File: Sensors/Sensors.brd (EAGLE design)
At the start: 101.6 x 53.3 mm, 28 parts, among them J10 JST_CONNECTOR, J11 JST_CONNECTOR, J2 JST_CONNECTOR, J5 JST_CONNECTOR, J6 JST_CONNECTOR, J7 JST_CONNECTOR, J8 JST_CONNECTOR, J9 JST_CONNECTOR

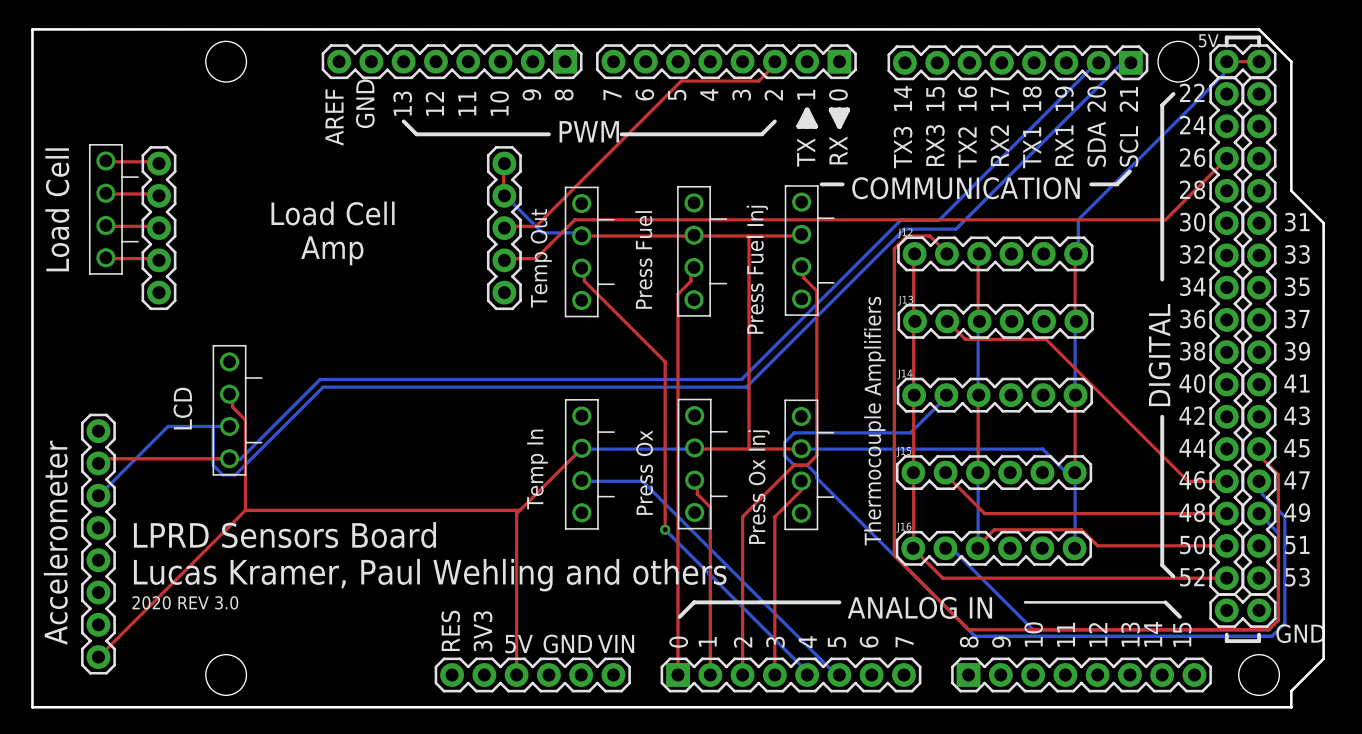
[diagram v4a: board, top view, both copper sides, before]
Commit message: Some minor tweaks to the layout
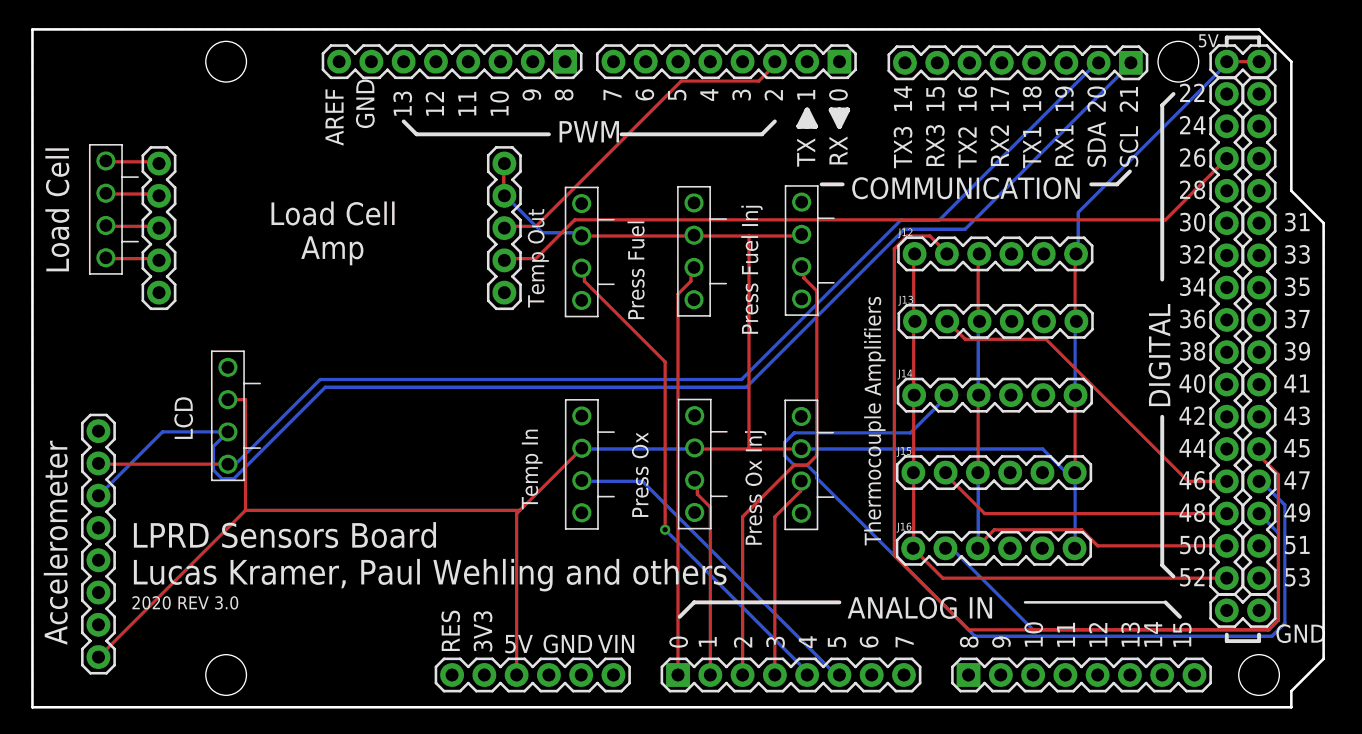
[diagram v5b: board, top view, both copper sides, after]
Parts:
- moved J11 0.45 mm to (15.4, 24.2)
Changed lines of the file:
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@@
 Lucas Kramer, Paul Wehling and others</text>
 <text x="7.7724" y="7.7089" size="1.016" layer="21" font="vector" ratio="15">2020 REV 3.0</text>
-<text x="48.7553" y="31.2039" size="1.27" layer="21" font="vector" ratio="15" rot="R90">Press Fuel</text>
-<text x="48.8061" y="14.986" size="1.27" layer="21" font="vector" ratio="15" rot="R90">Press Ox</text>
-<text x="40.5003" y="31.4579" size="1.27" layer="21" font="vector" ratio="15" rot="R90">Temp Out</text>
-<text x="40.1955" y="15.5829" size="1.27" layer="21" font="vector" ratio="15" rot="R90">Temp In</text>
+<text x="48.1457" y="30.3911" size="1.27" layer="21" font="vector" ratio="15" rot="R90">Press Fuel</text>
+<text x="48.4632" y="14.8209" size="1.27" layer="21" font="vector" ratio="15" rot="R90">Press Ox</text>
+<text x="40.2717" y="31.4579" size="1.27" layer="21" font="vector" ratio="15" rot="R90">Temp Out</text>
+<text x="39.7764" y="15.5829" size="1.27" layer="21" font="vector" ratio="15" rot="R90">Temp In</text>
 <text x="23.6474" y="35.2806" size="1.778" layer="21" font="vector" ratio="15" align="bottom-center">Load Cell
 Amp</text>
 <text x="2.8702" y="34.0868" size="1.778" layer="21" font="vector" ratio="15" rot="R90">Load Cell</text>
 <text x="2.7432" y="4.9022" size="1.778" layer="21" font="vector" ratio="15" rot="R90">Accelerometer</text>
-<text x="57.5183" y="29.2354" size="1.27" layer="21" font="vector" ratio="15" rot="R90">Press Fuel Inj</text>
-<text x="57.658" y="12.7" size="1.27" layer="21" font="vector" ratio="15" rot="R90">Press Ox Inj</text>
-<text x="12.5476" y="21.6916" size="1.4224" layer="21" font="vector" ratio="15" rot="R90">LCD</text>
+<text x="57.0992" y="29.2354" size="1.27" layer="21" font="vector" ratio="15" rot="R90">Press Fuel Inj</text>
+<text x="57.3913" y="12.6365" size="1.27" layer="21" font="vector" ratio="15" rot="R90">Press Ox Inj</text>
+<text x="12.6111" y="20.9423" size="1.4224" layer="21" font="vector" ratio="15" rot="R90">LCD</text>
 <text x="66.7639" y="12.7381" size="1.27" layer="21" font="vector" ratio="15" rot="R90">Thermocouple Amplifiers</text>
 </plain>
@@
 <element name="J5" library="LPRD_RELAY" package="B4B-XH-A(LF)(SN)" value="JST_CONNECTOR" x="60.5282" y="37.211" smashed="yes" rot="R90"/>
 <element name="J10" library="LPRD_RELAY" package="B4B-XH-A(LF)(SN)" value="JST_CONNECTOR" x="60.5028" y="20.3454" smashed="yes" rot="R90"/>
-<element name="J11" library="LPRD_RELAY" package="B4B-XH-A(LF)(SN)" value="JST_CONNECTOR" x="15.5067" y="24.638" smashed="yes" rot="R90"/>
+<element name="J11" library="LPRD_RELAY" package="B4B-XH-A(LF)(SN)" value="JST_CONNECTOR" x="15.3797" y="24.2062" smashed="yes" rot="R90"/>
 <element name="J12" library="SparkFun-Connectors" library_urn="urn:adsk.eagle:library:513" package="1X06" package3d_urn="urn:adsk.eagle:package:38009/1" value="" x="69.4182" y="35.6743" smashed="yes">
 <attribute name="NAME" x="68.1482" y="37.0713" size="0.6096" layer="25" font="vector" ratio="20"/>
@@
 <wire x1="82.042" y1="35.56" x2="82.1182" y2="35.6743" width="0.254" layer="1"/>
 <wire x1="82.042" y1="30.48" x2="82.1436" y2="30.3657" width="0.254" layer="1"/>
-<wire x1="93.726" y1="49.784" x2="93.726" y2="50.8" width="0.254" layer="16"/>
-<wire x1="82.296" y1="38.354" x2="93.726" y2="49.784" width="0.254" layer="16"/>
-<wire x1="82.296" y1="35.814" x2="82.296" y2="38.354" width="0.254" layer="16"/>
+<wire x1="93.726" y1="50.3682" x2="93.726" y2="50.8" width="0.254" layer="16"/>
+<wire x1="82.296" y1="38.9382" x2="93.726" y2="50.3682" width="0.254" layer="16"/>
+<wire x1="82.296" y1="35.814" x2="82.296" y2="38.9382" width="0.254" layer="16"/>
 <wire x1="93.726" y1="50.8" x2="93.98" y2="50.8" width="0.254" layer="16"/>
 <wire x1="82.296" y1="35.814" x2="82.1182" y2="35.6743" width="0.254" layer="16"/>
@@
 <wire x1="82.042" y1="18.542" x2="82.0166" y2="18.4658" width="0.254" layer="1"/>
 <wire x1="82.042" y1="24.384" x2="82.0801" y2="24.5618" width="0.254" layer="1"/>
-<wire x1="15.748" y1="23.622" x2="15.748" y2="24.638" width="0.254" layer="1"/>
-<wire x1="16.764" y1="22.606" x2="15.748" y2="23.622" width="0.254" layer="1"/>
-<wire x1="16.764" y1="15.494" x2="16.764" y2="22.606" width="0.254" layer="1"/>
+<wire x1="16.764" y1="15.494" x2="16.764" y2="24.2062" width="0.254" layer="1"/>
 <wire x1="5.334" y1="4.064" x2="16.764" y2="15.494" width="0.254" layer="1"/>
-<wire x1="15.748" y1="24.638" x2="15.5067" y2="24.638" width="0.254" layer="1"/>
+<wire x1="16.764" y1="24.2062" x2="15.3797" y2="24.2062" width="0.254" layer="1"/>
 <wire x1="5.334" y1="4.064" x2="5.1943" y2="3.9497" width="0.254" layer="1"/>
 <wire x1="60.452" y1="37.084" x2="56.388" y2="37.084" width="0.254" layer="1"/>
@@
 <contactref element="J11" pad="P$1"/>
 <contactref element="J1" pad="2"/>
-<wire x1="5.588" y1="19.558" x2="15.5067" y2="19.558" width="0.254" layer="1"/>
-<wire x1="5.334" y1="19.304" x2="5.588" y2="19.558" width="0.254" layer="1"/>
-<wire x1="5.334" y1="19.304" x2="5.1943" y2="19.1897" width="0.254" layer="1"/>
+<wire x1="15.3797" y1="19.1262" x2="5.2578" y2="19.1262" width="0.254" layer="1"/>
+<wire x1="5.1943" y1="19.1897" x2="5.2578" y2="19.1262" width="0.254" layer="1"/>
 <wire x1="71.374" y1="38.354" x2="83.82" y2="50.8" width="0.254" layer="16"/>
 <wire x1="68.3641" y1="38.354" x2="71.374" y2="38.354" width="0.254" layer="16"/>
 <wire x1="55.8038" y1="25.7937" x2="68.3641" y2="38.354" width="0.254" layer="16"/>
-<wire x1="15.5067" y1="19.558" x2="15.5702" y2="19.4945" width="0.254" layer="16"/>
-<wire x1="16.3449" y1="19.4945" x2="15.5702" y2="19.4945" width="0.254" layer="16"/>
-<wire x1="22.6441" y1="25.7937" x2="16.3449" y2="19.4945" width="0.254" layer="16"/>
 <wire x1="55.8038" y1="25.7937" x2="22.6441" y2="25.7937" width="0.254" layer="16"/>
 <wire x1="83.82" y1="50.8" x2="83.8962" y2="50.7111" width="0.254" layer="16"/>
+<wire x1="22.6441" y1="25.7937" x2="15.9766" y2="19.1262" width="0.254" layer="16"/>
+<wire x1="15.9766" y1="19.1262" x2="15.3797" y2="19.1262" width="0.254" layer="16"/>
 </signal>
 <signal name="SCL">
@@
 <contactref element="J11" pad="P$2"/>
 <contactref element="J1" pad="3"/>
-<wire x1="10.668" y1="22.098" x2="14.224" y2="22.098" width="0.254" layer="16"/>
-<wire x1="14.224" y1="22.098" x2="15.5067" y2="22.098" width="0.254" layer="16"/>
-<wire x1="5.334" y1="16.764" x2="10.668" y2="22.098" width="0.254" layer="16"/>
 <wire x1="5.334" y1="16.764" x2="5.1943" y2="16.6497" width="0.254" layer="16"/>
-<wire x1="85.598" y1="50.546" x2="86.36" y2="50.546" width="0.254" layer="16"/>
-<wire x1="72.6694" y1="37.6174" x2="85.598" y2="50.546" width="0.254" layer="16"/>
-<wire x1="68.6054" y1="37.6174" x2="72.6694" y2="37.6174" width="0.254" layer="16"/>
+<wire x1="86.3219" y1="50.546" x2="86.36" y2="50.546" width="0.254" layer="16"/>
+<wire x1="73.3933" y1="37.6174" x2="86.3219" y2="50.546" width="0.254" layer="16"/>
+<wire x1="68.6054" y1="37.6174" x2="73.3933" y2="37.6174" width="0.254" layer="16"/>
 <wire x1="56.1721" y1="25.1841" x2="68.6054" y2="37.6174" width="0.254" layer="16"/>
-<wire x1="22.86" y1="25.1841" x2="56.1721" y2="25.1841" width="0.254" layer="16"/>
-<wire x1="15.9639" y1="18.288" x2="22.86" y2="25.1841" width="0.254" layer="16"/>
-<wire x1="14.986" y1="18.288" x2="15.9639" y2="18.288" width="0.254" layer="16"/>
-<wire x1="14.224" y1="19.05" x2="14.986" y2="18.288" width="0.254" layer="16"/>
-<wire x1="14.224" y1="22.098" x2="14.224" y2="19.05" width="0.254" layer="16"/>
+<wire x1="23.042746875" y1="25.1841" x2="56.1721" y2="25.1841" width="0.254" layer="16"/>
 <wire x1="86.36" y1="50.546" x2="86.4362" y2="50.7111" width="0.254" layer="16"/>
+<wire x1="15.3797" y1="21.6662" x2="10.2362" y2="21.6662" width="0.254" layer="16"/>
+<wire x1="10.2362" y1="21.6662" x2="5.334" y2="16.764" width="0.254" layer="16"/>
+<wire x1="23.042746875" y1="25.1841" x2="15.849846875" y2="17.9912" width="0.254" layer="16"/>
+<wire x1="15.849846875" y1="17.9912" x2="14.909553125" y2="17.9912" width="0.254" layer="16"/>
+<wire x1="14.909553125" y1="17.9912" x2="14.2447" y2="18.656053125" width="0.254" layer="16"/>
+<wire x1="14.2447" y1="18.656053125" x2="14.2447" y2="20.5312" width="0.254" layer="16"/>
+<wire x1="14.2447" y1="20.5312" x2="15.3797" y2="21.6662" width="0.254" layer="16"/>
 </signal>
 <signal name="D39">
@@
 <contactref element="J14" pad="2"/>
 <contactref element="JP8" pad="4"/>
-<wire x1="96.774" y1="16.764" x2="96.774" y2="17.78" width="0.254" layer="16"/>
-<wire x1="98.552" y1="14.986" x2="96.774" y2="16.764" width="0.254" layer="16"/>
-<wire x1="98.552" y1="6.604" x2="98.552" y2="14.986" width="0.254" layer="16"/>
+<wire x1="96.774" y1="17.6911" x2="96.774" y2="17.78" width="0.254" layer="16"/>
+<wire x1="98.552" y1="15.9131" x2="96.774" y2="17.6911" width="0.254" layer="16"/>
+<wire x1="98.552" y1="6.604" x2="98.552" y2="15.9131" width="0.254" layer="16"/>
 <wire x1="97.536" y1="5.588" x2="98.552" y2="6.604" width="0.254" layer="16"/>
 <wire x1="74.168" y1="5.588" x2="97.536" y2="5.588" width="0.254" layer="16"/>

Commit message: Fix thermocouple amp spacing
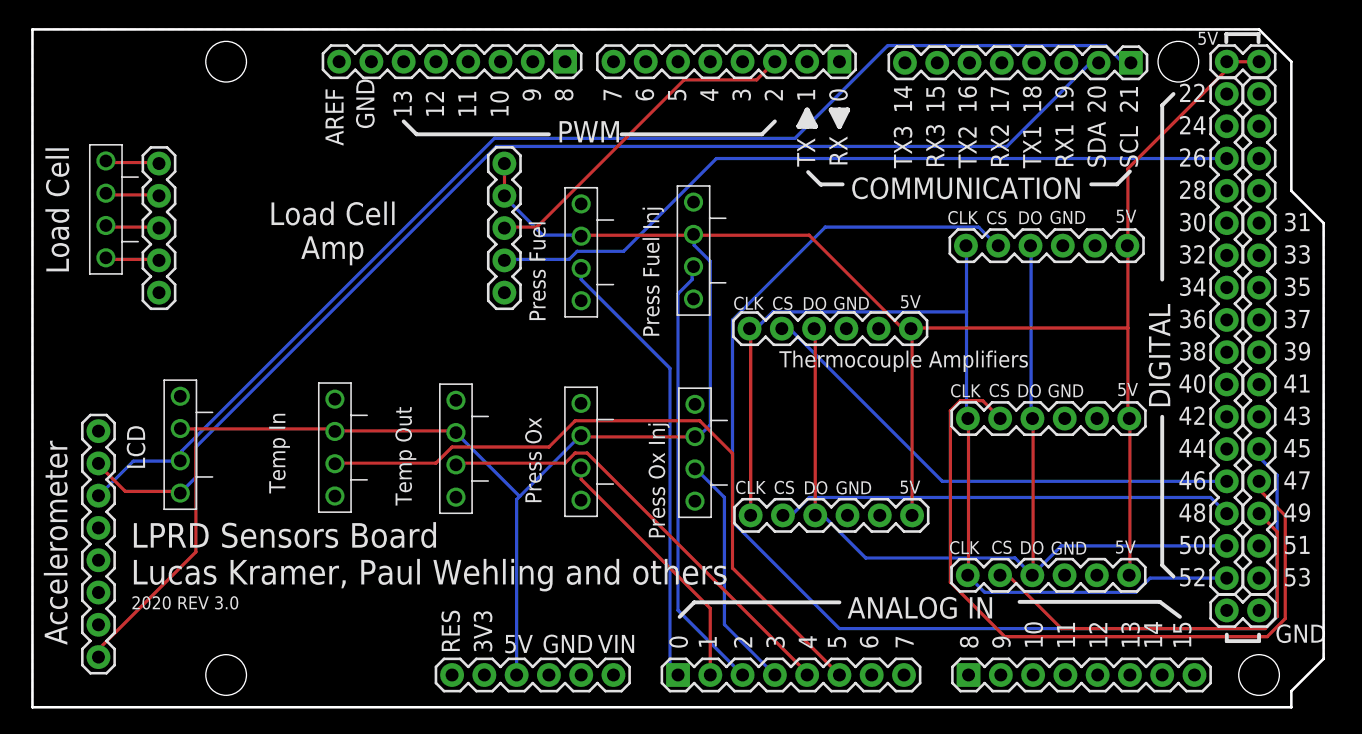
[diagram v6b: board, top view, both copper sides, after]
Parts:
- moved J7 19.5 mm to (23.8, 21.7)
- moved J6 18.4 mm to (33.3, 21.6)
- moved J15 13.2 mm to (56.5, 15.1)
- moved J13 13.0 mm to (56.4, 29.8)
- moved J9 8.99 mm to (43.2, 21.4)
- moved J8 8.88 mm to (43.2, 37.1)
- moved J5 8.51 mm to (52.0, 37.2)
- moved J10 8.42 mm to (52.1, 21.3)
- moved J16 4.79 mm to (73.6, 10.4)
- moved J14 4.61 mm to (73.6, 22.7)
- moved J11 4.38 mm to (11.6, 21.9)
- moved J12 4.09 mm to (73.5, 36.3)
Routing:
- net MISO: track 44.1 -> 76.1 mm
- net SCK: track 48.9 -> 79.8 mm
- net TEMPERATURE_IN: track 27.0 -> 54.7 mm
- net THERMO_CS1: track 76.4 -> 100.9 mm
- net 5V: track 197.9 -> 214.4 mm
- net THERMO_CS3: track 73.4 -> 58.7 mm
- net THERMO_CS2: track 27.2 -> 40.0 mm
- net THERMO_CS4: track 23.5 -> 36.1 mm
- net THERMO_CS5: track 38.2 -> 32.6 mm
- net SCL: track 101.8 -> 96.9 mm
- net PRESSURE_OX: track 15.9 -> 20.5 mm
- net TEMPERATURE_OUT: track 39.5 -> 35.4 mm, vias 1 -> 0
- net SDA: track 91.9 -> 95.2 mm
- net PRESSURE_OX_INJ: track 16.1 -> 18.9 mm
- net PRESSURE_FUEL: track 32.7 -> 35.1 mm
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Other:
- board text added: "CLK"
- board text added: "CS"
- board text added: "DO"

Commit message: Some minor adjustments to sensors board layout for future revisions, based on lessons learned from populating v3.0 (not routed yet)
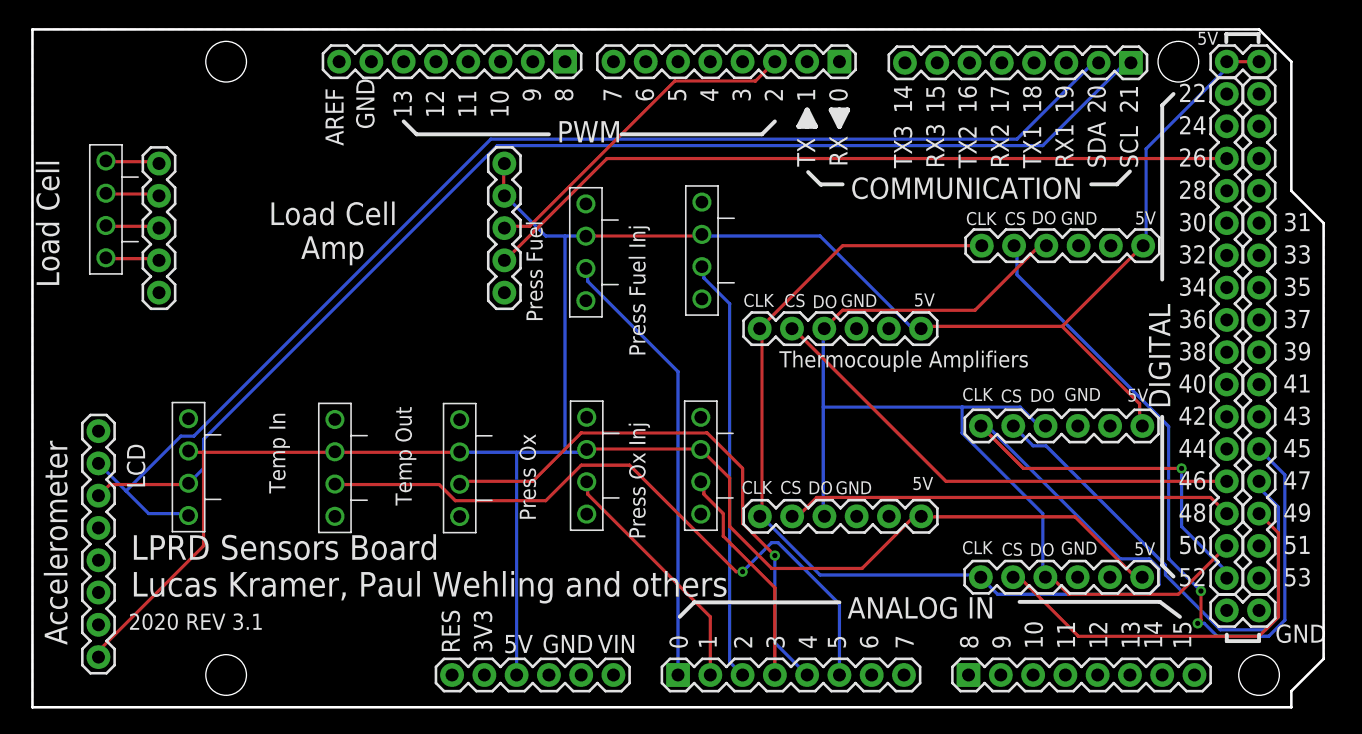
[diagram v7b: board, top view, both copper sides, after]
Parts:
- moved J11 1.88 mm to (12.3, 20.2)
- moved J7 1.60 mm to (23.8, 20.1)
- moved J6 1.55 mm to (33.6, 20.1)
- moved J12 1.24 mm to (74.7, 36.3)
- moved J14 1.18 mm to (74.6, 22.1)
- moved J9 1.18 mm to (43.6, 20.3)
- moved J10 1.11 mm to (52.6, 20.3)
- moved J16 1.04 mm to (74.6, 10.2)
- moved J13 0.80 mm to (57.2, 29.8)
- moved J15 0.73 mm to (57.2, 15.0)
- moved J5 0.66 mm to (52.7, 37.2)
- moved J8 0.37 mm to (43.5, 37.1)
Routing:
- net THERMO_CS1: track 100.9 -> 58.2 mm, vias 0 -> 2
- net SCK: track 79.8 -> 116.6 mm, vias 0 -> 1
- net THERMO_CS3: track 58.7 -> 39.7 mm
- net 5V: track 214.4 -> 229.4 mm
- net MISO: track 76.1 -> 85.6 mm
- net TEMPERATURE_OUT: track 35.4 -> 43.5 mm, vias 0 -> 1
- net SDA: track 95.2 -> 99.3 mm
- net PRESSURE_FUEL_INJ: track 34.8 -> 33.5 mm
- net PRESSURE_OX: track 20.5 -> 19.2 mm
- net TEMPERATURE_IN: track 54.7 -> 53.4 mm, vias 0 -> 1
- net PRESSURE_OX_INJ: track 18.9 -> 17.6 mm
- net THERMO_CS2: track 40.0 -> 39.2 mm
- net THERMO_CS4: track 36.1 -> 35.4 mm
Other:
- board text added: "2020 REV 3.1"
- board text removed: "2020 REV 3.0"

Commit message: Remove partial broken routing
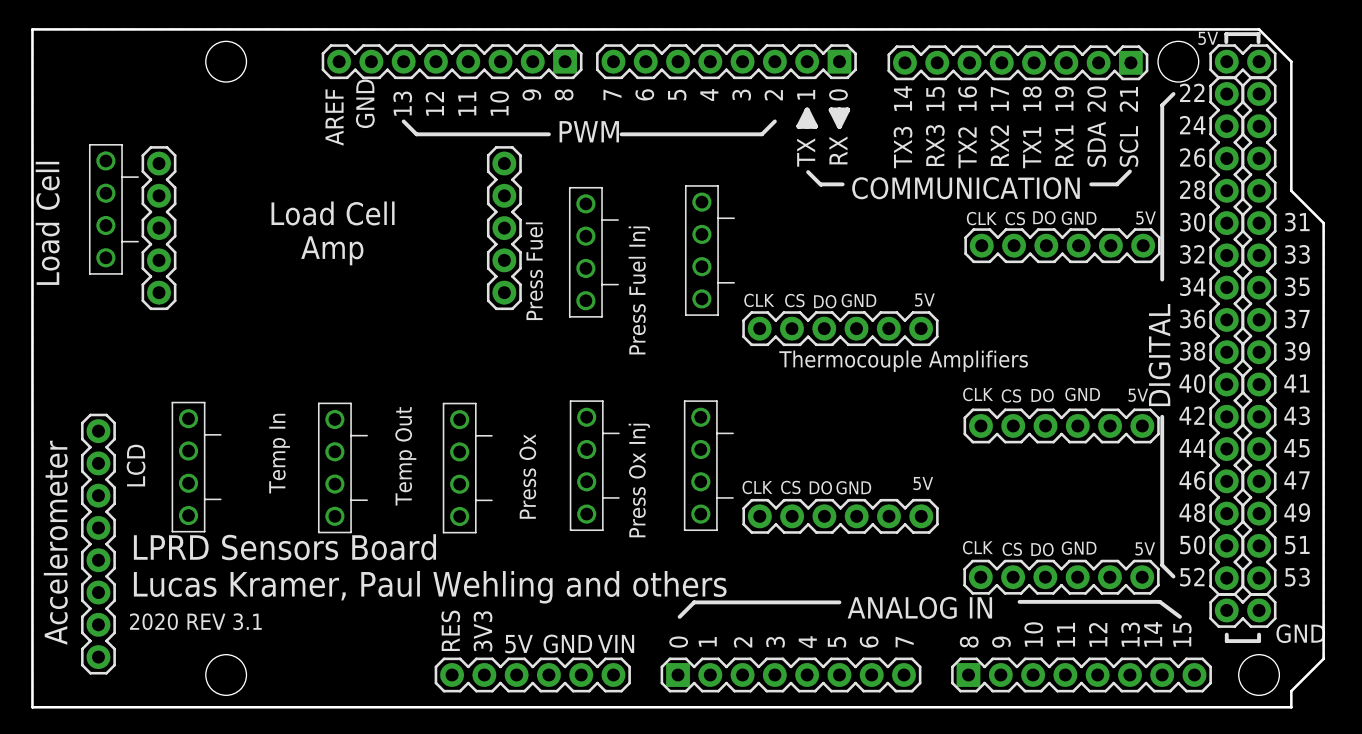
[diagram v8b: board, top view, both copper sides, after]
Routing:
- net 5V: track 229.4 -> 0.00 mm
- net SCK: track 116.6 -> 0.00 mm, vias 1 -> 0
- net SDA: track 99.3 -> 0.00 mm
- net SCL: track 96.7 -> 0.00 mm
- net MISO: track 85.6 -> 0.00 mm
- net FORCE_CLK: track 60.2 -> 0.00 mm
- net THERMO_CS1: track 58.2 -> 0.00 mm, vias 2 -> 0
- net TEMPERATURE_IN: track 53.4 -> 0.00 mm, vias 1 -> 0
- net TEMPERATURE_OUT: track 43.5 -> 0.00 mm, vias 1 -> 0
- net THERMO_CS3: track 39.7 -> 0.00 mm
- net THERMO_CS2: track 39.2 -> 0.00 mm
- net THERMO_CS4: track 35.4 -> 0.00 mm
- net PRESSURE_FUEL: track 35.0 -> 0.00 mm
- net PRESSURE_FUEL_INJ: track 33.5 -> 0.00 mm
- net THERMO_CS5: track 32.2 -> 0.00 mm
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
